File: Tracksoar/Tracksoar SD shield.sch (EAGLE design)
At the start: 4 parts, among them U1 EEPROM-I2CSMD

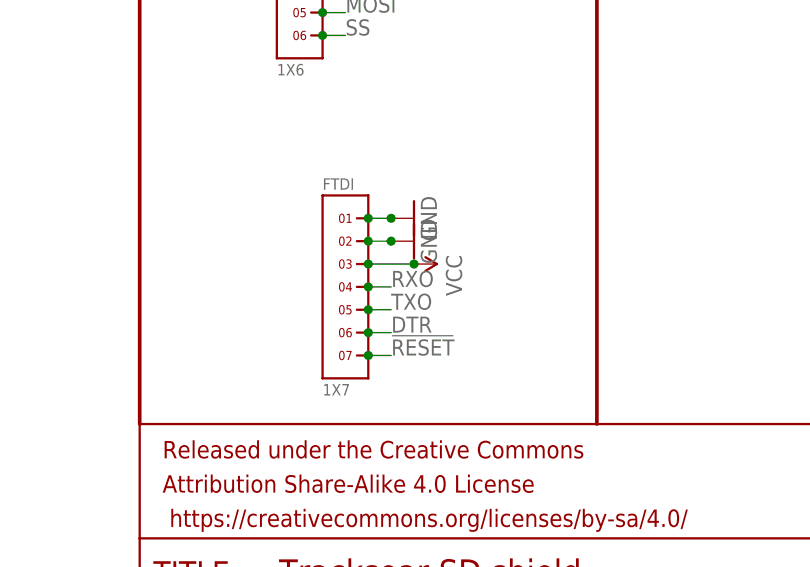
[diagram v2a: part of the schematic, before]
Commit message: resolved 1.6.5+ compiling issues
resolved issues in afsk_avr.cpp / h that prevented the firmware from
compiling in 1.6.5+
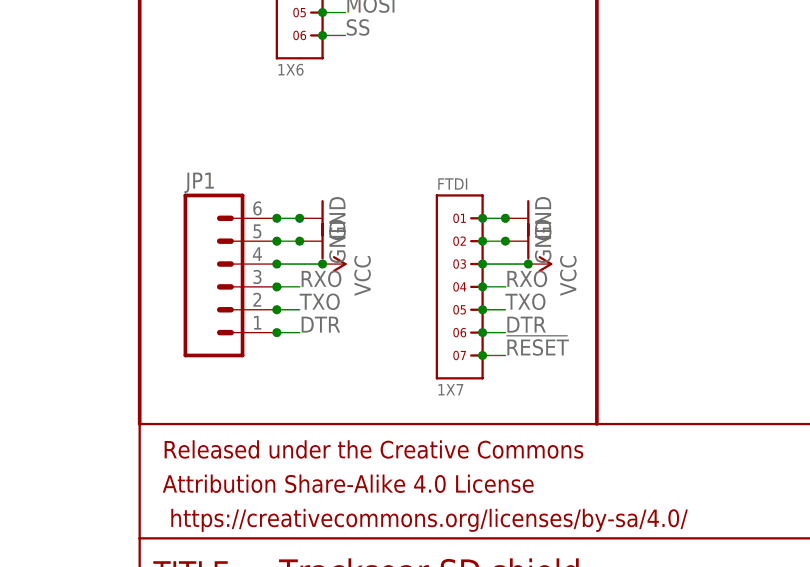
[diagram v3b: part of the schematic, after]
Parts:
- added JP1: (no value), SparkFun-Connectors:M06LOCK_LONGPADS
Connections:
- net DTR: now also JP1.1
- net GND: now also JP1.5, JP1.6
- net RXO: now also JP1.3
- net TXO: now also JP1.2
- net VCC: now also JP1.4
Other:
- moved on the sheet: FTDI
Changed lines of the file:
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@@
 <?xml version="1.0" encoding="utf-8"?>
 <!DOCTYPE eagle SYSTEM "eagle.dtd">
-<eagle version="7.3.0">
+<eagle version="7.5.0">
 <drawing>
 <settings>
@@
 <part name="SPI/I2C" library="headers(2mm)" deviceset="1X6" device=""/>
 <part name="U1" library="SparkFun-DigitalIC" deviceset="EEPROM-I2C" device="SMD"/>
+<part name="GND1" library="SparkFun-Aesthetics" deviceset="GND" device=""/>
+<part name="GND2" library="SparkFun-Aesthetics" deviceset="GND" device=""/>
+<part name="SUPPLY1" library="SparkFun-Aesthetics" deviceset="VCC" device=""/>
+<part name="JP1" library="SparkFun-Connectors" deviceset="M06" device="LOCK_LONGPADS"/>
 </parts>
 <sheets>
@@
 </plain>
 <instances>
-<instance part="GND22" gate="1" x="177.8" y="58.42" rot="R90"/>
-<instance part="SUPPLY9" gate="G$1" x="177.8" y="53.34" rot="R270"/>
+<instance part="GND22" gate="1" x="190.5" y="58.42" rot="R90"/>
+<instance part="SUPPLY9" gate="G$1" x="190.5" y="53.34" rot="R270"/>
 <instance part="FRAME1" gate="G$1" x="0" y="0"/>
 <instance part="FRAME1" gate="G$2" x="147.32" y="0" smashed="yes">
@@
 <attribute name="DRAWING_NAME" x="162.814" y="17.78" size="2.7432" layer="94" font="vector"/>
 </instance>
-<instance part="GND10" gate="1" x="177.8" y="55.88" rot="R90"/>
-<instance part="FTDI" gate="G$1" x="170.18" y="50.8"/>
+<instance part="GND10" gate="1" x="190.5" y="55.88" rot="R90"/>
+<instance part="FTDI" gate="G$1" x="182.88" y="50.8"/>
 <instance part="SPI/I2C" gate="G$1" x="165.1" y="83.82"/>
 <instance part="U1" gate="G$1" x="78.74" y="99.06"/>
+<instance part="GND1" gate="1" x="167.64" y="58.42" rot="R90"/>
+<instance part="GND2" gate="1" x="167.64" y="55.88" rot="R90"/>
+<instance part="SUPPLY1" gate="G$1" x="167.64" y="53.34" rot="R270"/>
+<instance part="JP1" gate="G$1" x="157.48" y="50.8"/>
 </instances>
 <busses>
@@
 <net name="GND" class="0">
 <segment>
-<wire x1="172.72" y1="58.42" x2="175.26" y2="58.42" width="0.1524" layer="91"/>
+<wire x1="185.42" y1="58.42" x2="187.96" y2="58.42" width="0.1524" layer="91"/>
 <pinref part="GND22" gate="1" pin="GND"/>
-<junction x="175.26" y="58.42"/>
+<junction x="187.96" y="58.42"/>
 <pinref part="FTDI" gate="G$1" pin="1"/>
-<junction x="172.72" y="58.42"/>
-</segment>
-<segment>
-<wire x1="172.72" y1="55.88" x2="175.26" y2="55.88" width="0.1524" layer="91"/>
+<junction x="185.42" y="58.42"/>
+</segment>
+<segment>
+<wire x1="185.42" y1="55.88" x2="187.96" y2="55.88" width="0.1524" layer="91"/>
 <pinref part="GND10" gate="1" pin="GND"/>
-<junction x="175.26" y="55.88"/>
+<junction x="187.96" y="55.88"/>
 <pinref part="FTDI" gate="G$1" pin="2"/>
-<junction x="172.72" y="55.88"/>
+<junction x="185.42" y="55.88"/>
 </segment>
 <segment>
@@
 <junction x="66.04" y="96.52"/>
 </segment>
+<segment>
+<wire x1="162.56" y1="58.42" x2="165.1" y2="58.42" width="0.1524" layer="91"/>
+<pinref part="GND1" gate="1" pin="GND"/>
+<junction x="165.1" y="58.42"/>
+<pinref part="JP1" gate="G$1" pin="6"/>
+<junction x="162.56" y="58.42"/>
+</segment>
+<segment>
+<wire x1="162.56" y1="55.88" x2="165.1" y2="55.88" width="0.1524" layer="91"/>
+<pinref part="GND2" gate="1" pin="GND"/>
+<junction x="165.1" y="55.88"/>
+<pinref part="JP1" gate="G$1" pin="5"/>
+<junction x="162.56" y="55.88"/>
+</segment>
 </net>
 <net name="VCC" class="0">
 <segment>
-<wire x1="172.72" y1="53.34" x2="177.8" y2="53.34" width="0.1524" layer="91"/>
+<wire x1="185.42" y1="53.34" x2="190.5" y2="53.34" width="0.1524" layer="91"/>
 <pinref part="SUPPLY9" gate="G$1" pin="VCC"/>
-<junction x="177.8" y="53.34"/>
+<junction x="190.5" y="53.34"/>
 <pinref part="FTDI" gate="G$1" pin="3"/>
-<junction x="172.72" y="53.34"/>
+<junction x="185.42" y="53.34"/>
 </segment>
 <segment>
@@
 <junction x="91.44" y="104.14"/>
 </segment>
+<segment>
+<wire x1="162.56" y1="53.34" x2="167.64" y2="53.34" width="0.1524" layer="91"/>
+<pinref part="SUPPLY1" gate="G$1" pin="VCC"/>
+<junction x="167.64" y="53.34"/>
+<pinref part="JP1" gate="G$1" pin="4"/>
+<junction x="162.56" y="53.34"/>
+</segment>
 </net>
 <net name="DTR" class="0">
 <segment>
-<wire x1="172.72" y1="45.72" x2="175.26" y2="45.72" width="0.1524" layer="91"/>
-<label x="175.26" y="45.72" size="1.778" layer="95"/>
+<wire x1="185.42" y1="45.72" x2="187.96" y2="45.72" width="0.1524" layer="91"/>
+<label x="187.96" y="45.72" size="1.778" layer="95"/>
 <pinref part="FTDI" gate="G$1" pin="6"/>
-<junction x="172.72" y="45.72"/>
+<junction x="185.42" y="45.72"/>
+<label x="165.1" y="45.72" size="1.778" layer="95"/>
+</segment>
+<segment>
+<wire x1="162.56" y1="45.72" x2="165.1" y2="45.72" width="0.1524" layer="91"/>
+<pinref part="JP1" gate="G$1" pin="1"/>
+<junction x="162.56" y="45.72"/>
 </segment>
 </net>
 <net name="RXO" class="0">
 <segment>
-<wire x1="172.72" y1="50.8" x2="175.26" y2="50.8" width="0.1524" layer="91"/>
-<label x="175.26" y="50.8" size="1.778" layer="95"/>
+<wire x1="185.42" y1="50.8" x2="187.96" y2="50.8" width="0.1524" layer="91"/>
+<label x="187.96" y="50.8" size="1.778" layer="95"/>
 <pinref part="FTDI" gate="G$1" pin="4"/>
-<junction x="172.72" y="50.8"/>
+<junction x="185.42" y="50.8"/>
+<label x="165.1" y="50.8" size="1.778" layer="95"/>
+</segment>
+<segment>
+<wire x1="162.56" y1="50.8" x2="165.1" y2="50.8" width="0.1524" layer="91"/>
+<pinref part="JP1" gate="G$1" pin="3"/>
+<junction x="162.56" y="50.8"/>
 </segment>
 </net>
 <net name="TXO" class="0">
 <segment>
-<wire x1="172.72" y1="48.26" x2="175.26" y2="48.26" width="0.1524" layer="91"/>
-<label x="175.26" y="48.26" size="1.778" layer="95"/>
+<wire x1="185.42" y1="48.26" x2="187.96" y2="48.26" width="0.1524" layer="91"/>
+<label x="187.96" y="48.26" size="1.778" layer="95"/>
 <pinref part="FTDI" gate="G$1" pin="5"/>
-<junction x="172.72" y="48.26"/>
+<junction x="185.42" y="48.26"/>
+<label x="165.1" y="48.26" size="1.778" layer="95"/>
+</segment>
+<segment>
+<wire x1="162.56" y1="48.26" x2="165.1" y2="48.26" width="0.1524" layer="91"/>
+<pinref part="JP1" gate="G$1" pin="2"/>
+<junction x="162.56" y="48.26"/>
 </segment>
 </net>
@@
 <net name="!RESET" class="0">
 <segment>
-<wire x1="172.72" y1="43.18" x2="175.26" y2="43.18" width="0.1524" layer="91"/>
-<label x="175.26" y="43.18" size="1.778" layer="95"/>
+<wire x1="185.42" y1="43.18" x2="187.96" y2="43.18" width="0.1524" layer="91"/>
+<label x="187.96" y="43.18" size="1.778" layer="95"/>
 <pinref part="FTDI" gate="G$1" pin="7"/>
-<junction x="172.72" y="43.18"/>
-</segment>
-</net>
+<junction x="185.42" y="43.18"/>
+</segment>
+</net>

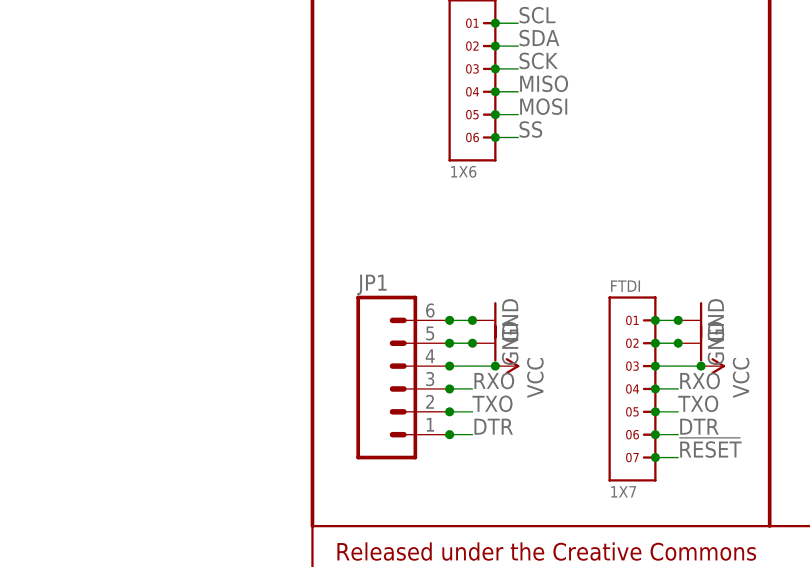
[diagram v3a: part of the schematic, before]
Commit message: added eeprom silkscreen
added silkscreen markings to the EEPROM FTDI connector
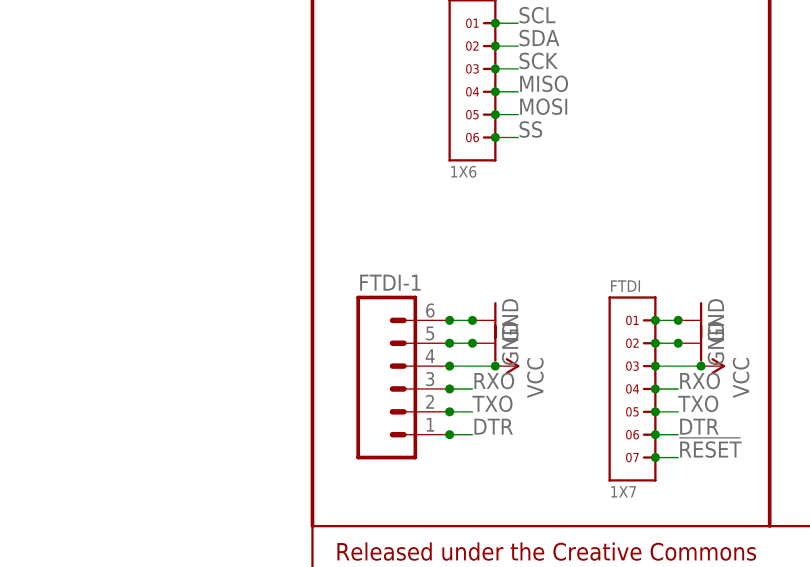
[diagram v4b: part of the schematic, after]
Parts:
- renumbered JP1 to FTDI-1
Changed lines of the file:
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@@
 <?xml version="1.0" encoding="utf-8"?>
 <!DOCTYPE eagle SYSTEM "eagle.dtd">
-<eagle version="7.5.0">
+<eagle version="7.3.0">
 <drawing>
 <settings>
@@
 <part name="GND2" library="SparkFun-Aesthetics" deviceset="GND" device=""/>
 <part name="SUPPLY1" library="SparkFun-Aesthetics" deviceset="VCC" device=""/>
-<part name="JP1" library="SparkFun-Connectors" deviceset="M06" device="LOCK_LONGPADS"/>
+<part name="FTDI-1" library="SparkFun-Connectors" deviceset="M06" device="LOCK_LONGPADS"/>
 </parts>
 <sheets>
@@
 <instance part="GND2" gate="1" x="167.64" y="55.88" rot="R90"/>
 <instance part="SUPPLY1" gate="G$1" x="167.64" y="53.34" rot="R270"/>
-<instance part="JP1" gate="G$1" x="157.48" y="50.8"/>
+<instance part="FTDI-1" gate="G$1" x="157.48" y="50.8"/>
 </instances>
 <busses>
@@
 <pinref part="GND1" gate="1" pin="GND"/>
 <junction x="165.1" y="58.42"/>
-<pinref part="JP1" gate="G$1" pin="6"/>
+<pinref part="FTDI-1" gate="G$1" pin="6"/>
 <junction x="162.56" y="58.42"/>
 </segment>
@@
 <pinref part="GND2" gate="1" pin="GND"/>
 <junction x="165.1" y="55.88"/>
-<pinref part="JP1" gate="G$1" pin="5"/>
+<pinref part="FTDI-1" gate="G$1" pin="5"/>
 <junction x="162.56" y="55.88"/>
 </segment>
@@
 <pinref part="SUPPLY1" gate="G$1" pin="VCC"/>
 <junction x="167.64" y="53.34"/>
-<pinref part="JP1" gate="G$1" pin="4"/>
+<pinref part="FTDI-1" gate="G$1" pin="4"/>
 <junction x="162.56" y="53.34"/>
 </segment>
@@
 <segment>
 <wire x1="162.56" y1="45.72" x2="165.1" y2="45.72" width="0.1524" layer="91"/>
-<pinref part="JP1" gate="G$1" pin="1"/>
+<pinref part="FTDI-1" gate="G$1" pin="1"/>
 <junction x="162.56" y="45.72"/>
 </segment>
@@
 <segment>
 <wire x1="162.56" y1="50.8" x2="165.1" y2="50.8" width="0.1524" layer="91"/>
-<pinref part="JP1" gate="G$1" pin="3"/>
+<pinref part="FTDI-1" gate="G$1" pin="3"/>
 <junction x="162.56" y="50.8"/>
 </segment>
@@
 <segment>
 <wire x1="162.56" y1="48.26" x2="165.1" y2="48.26" width="0.1524" layer="91"/>
-<pinref part="JP1" gate="G$1" pin="2"/>
+<pinref part="FTDI-1" gate="G$1" pin="2"/>
 <junction x="162.56" y="48.26"/>
 </segment>
